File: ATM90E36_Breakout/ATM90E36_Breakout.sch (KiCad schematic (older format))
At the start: 70 parts, among them IC1 ATM90E36, Q1 FA-128

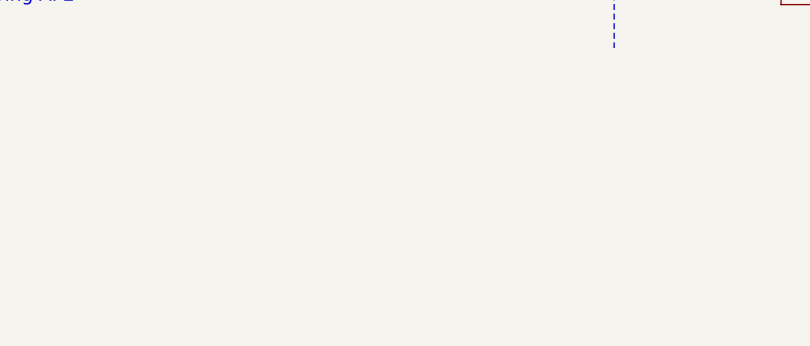
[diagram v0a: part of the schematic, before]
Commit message: Fix up silk screens
Signed-off-by: Tisham Dhar <whatnickd@gmail.com>
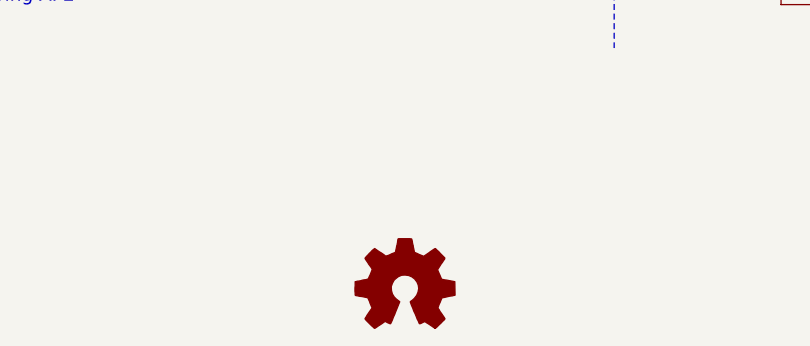
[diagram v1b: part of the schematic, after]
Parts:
- added LOGO1: Logo_Open_Hardware_Small, ATM90E36_Breakout:OSHW-LOGO-M, symbol Graphic:Logo_Open_Hardware_Small
- IC1: manf# (none) -> ATM90E36A-AU-R
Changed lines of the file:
@@
 F 2 "ATM90E36_Breakout:TQFP48" H 7200 3800 50  0001 C CNN
 F 3 "" H 7200 3800 50  0001 C CNN
+F 4 "	ATM90E36A-AU-R" H 7200 3800 50  0001 C CNN "manf#"
 	1    7200 3800
 	1    0    0    -1
@@
 Wire Notes Line
 	9420 750  9420 6990
+$Comp
+L Graphic:Logo_Open_Hardware_Small LOGO1
+U 1 1 5E08577C
+P 8505 8045
+F 0 "LOGO1" H 8505 8320 50  0001 C CNN
+F 1 "Logo_Open_Hardware_Small" H 8505 7820 50  0001 C CNN
+F 2 "ATM90E36_Breakout:OSHW-LOGO-M" H 8505 8045 50  0001 C CNN
+F 3 "~" H 8505 8045 50  0001 C CNN
+	1    8505 8045
+	1    0    0    -1
+$EndComp
 $EndSCHEMATC

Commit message: Add full BOM and Gerbers
Signed-off-by: Tisham Dhar <whatnickd@gmail.com>
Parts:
- added Hole0, Hole1, Hole2, Hole3: MountingHole, MountingHole:MountingHole_2.2mm_M2, symbol Mechanical:MountingHole
- C1, C10, C11, C14, C16, C2, C20, C3, C4, C5, C6, C7, C8, C9: manf# (none) -> C0603C183K5RACTU
- C12, C19: manf# (none) -> GRM21BR61E106MA73L
- C13, C15, C17, C18, C21: manf# (none) -> C0603C104K5RAC3190
- CTA1, CTB1, CTC1, CTN1: manf# (none) -> ST-PJ-312
- DMA1, JP1, JP2, JP3, LOGO1, PM0, PM1: DNP (none) -> (none)
- LED1: manf# (none) -> LTST-C193KRKT-5A
- LED2: value GRN -> RED; manf# (none) -> LTST-C193KRKT-5A
- LED3: value BLU -> RED; manf# (none) -> LTST-C193KRKT-5A
- LED4: value YEL -> RED; manf# (none) -> LTST-C193KRKT-5A
- Q1: manf# (none) -> FA-128 16.00M-A0NNNNHB0REB
- R1, R15, R16, R17, R18, R2, R3, R4: manf# (none) -> CRL0603-FW-2R40ELF
- R10, R12, R14: manf# (none) -> RC0603FR-07100KL
- R11, R13, R19, R20, R21, R22, R23, R24, R25, R5, R6, R7, R8, R9: manf# (none) -> RT0603FRE071KL
- R26: manf# (none) -> SR0603KR-7W10KL
- R27: manf# (none) -> YC164-JR-071KL
- R36: manf# (none) -> YC164-JR-0710KL
- UAUB1, UCUN1: manf# (none) -> 20020327-C021B01LF
- ZX0, ZX2: value ZX0 -> ZX; DNP (none) -> (none)
- ZX1: value ZX1 -> ZX; DNP (none) -> (none)

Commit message: Update parts for availability
Signed-off-by: Tisham Dhar <whatnickd@gmail.com>
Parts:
- CTA1, CTB1, CTC1, CTN1: manf# ST-PJ-312 -> ST-PJ-342
- Q1: manf# FA-128 16.00M-A0NNNNHB0REB -> ECS-160-10-36-CKM-TR
- R26: manf# SR0603KR-7W10KL -> RC0201JR-0710KL
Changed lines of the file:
@@
 F 2 "ATM90E36_Breakout:R0603" H 7390 1100 50  0001 C CNN
 F 3 "" H 7390 1100 50  0001 C CNN
-F 4 "SR0603KR-7W10KL" H 7390 1100 50  0001 C CNN "manf#"
+F 4 "RC0201JR-0710KL" H 7390 1100 50  0001 C CNN "manf#"
 	1    7390 1100
 	-1   0    0    1
@@
 F 2 "ATM90E36_Breakout:FA-128" H 7460 5890 50  0001 C CNN
 F 3 "" H 7460 5890 50  0001 C CNN
-F 4 "FA-128 16.00M-A0NNNNHB0REB" H 7460 5890 50  0001 C CNN "manf#"
+F 4 "ECS-160-10-36-CKM-TR" H 7460 5890 50  0001 C CNN "manf#"
 	1    7460 5890
 	1    0    0    -1
@@
 F 2 "ATM90E36_Breakout:AUDIO6P-SMD-3.5-14.0X6.4X5.0MM" H 10060 1500 50  0001 C CNN
 F 3 "" H 10060 1500 50  0001 C CNN
-F 4 "ST-PJ-312" H 10060 1500 50  0001 C CNN "manf#"
+F 4 "ST-PJ-342" H 10060 1500 50  0001 C CNN "manf#"
 	1    10060 1500
 	0    -1   -1   0
@@
 F 2 "ATM90E36_Breakout:AUDIO6P-SMD-3.5-14.0X6.4X5.0MM" H 11100 1500 50  0001 C CNN
 F 3 "" H 11100 1500 50  0001 C CNN
-F 4 "ST-PJ-312" H 11100 1500 50  0001 C CNN "manf#"
+F 4 "ST-PJ-342" H 11100 1500 50  0001 C CNN "manf#"
 	1    11100 1500
 	0    -1   -1   0
@@
 F 2 "ATM90E36_Breakout:AUDIO6P-SMD-3.5-14.0X6.4X5.0MM" H 10000 3120 50  0001 C CNN
 F 3 "" H 10000 3120 50  0001 C CNN
-F 4 "ST-PJ-312" H 10000 3120 50  0001 C CNN "manf#"
+F 4 "ST-PJ-342" H 10000 3120 50  0001 C CNN "manf#"
 	1    10000 3120
 	0    -1   -1   0
@@
 F 2 "ATM90E36_Breakout:AUDIO6P-SMD-3.5-14.0X6.4X5.0MM" H 11040 3110 50  0001 C CNN
 F 3 "" H 11040 3110 50  0001 C CNN
-F 4 "ST-PJ-312" H 11040 3110 50  0001 C CNN "manf#"
+F 4 "ST-PJ-342" H 11040 3110 50  0001 C CNN "manf#"
 	1    11040 3110
 	0    -1   -1   0

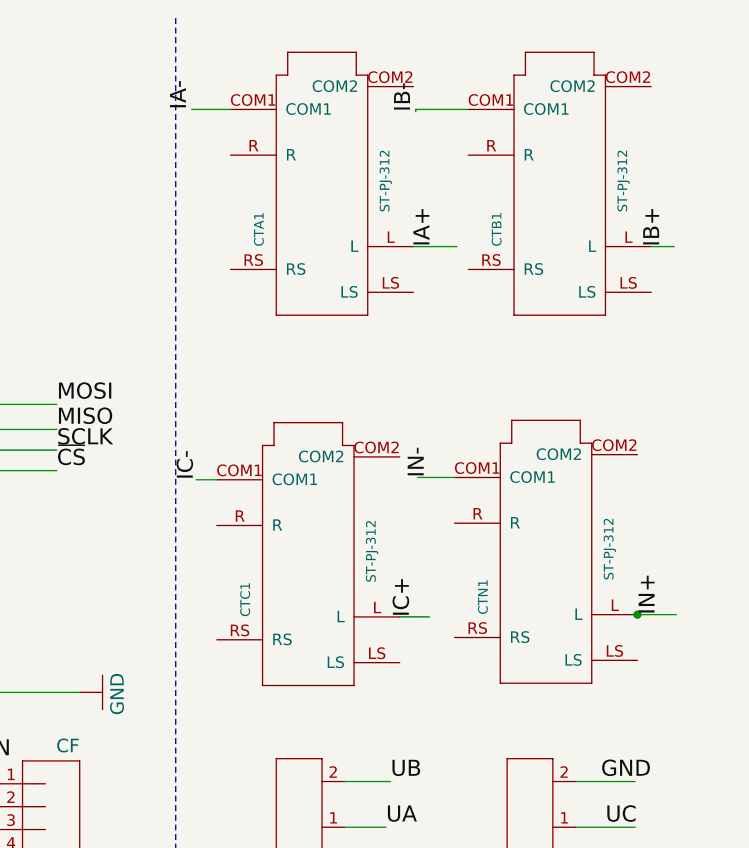
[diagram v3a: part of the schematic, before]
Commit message: Updated Stereojacks to mainstream ones
Signed-off-by: Tisham Dhar <whatnickd@gmail.com>
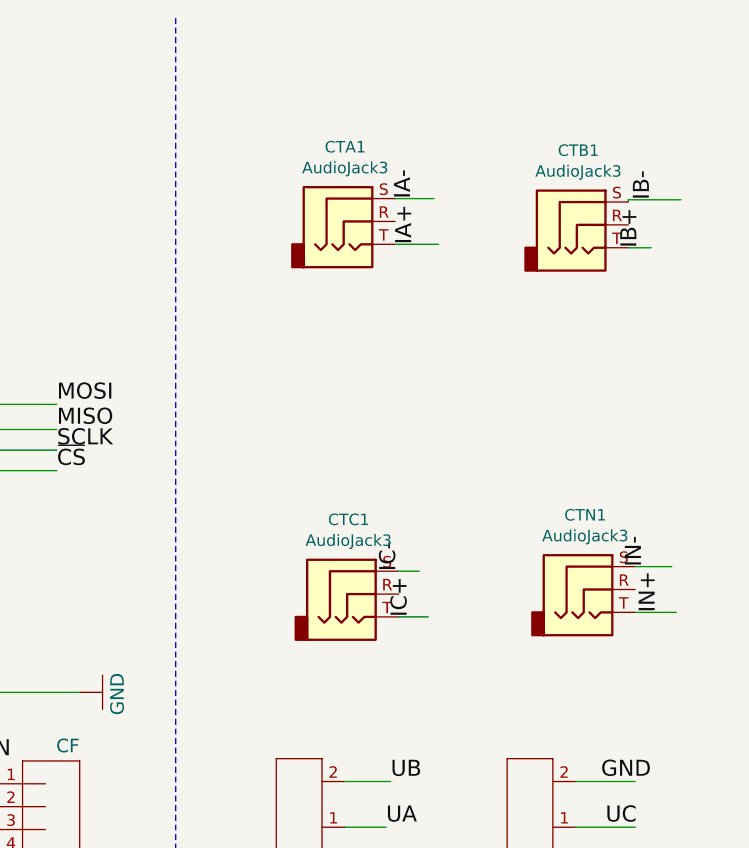
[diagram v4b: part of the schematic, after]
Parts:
- removed CTA1, CTB1, CTC1, CTN1: ST-PJ-312, ATM90E36_Breakout:AUDIO6P-SMD-3.5-14.0X6.4X5.0MM, symbol ATM90E36_Breakout-eagle-import:AUDIO-JACK-6P-SMD(ST-PJ-312)
- added CTA1, CTB1, CTC1, CTN1: AudioJack3, Connector_Audio:Jack_3.5mm_CUI_SJ-3523-SMT_Horizontal, symbol Connector:AudioJack3
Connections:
- wire segments 282 -> 281
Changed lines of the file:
@@
 IB-
 Wire Wire Line
-	10700 1150 10470 1150
-Wire Wire Line
-	10470 1150 10470 1160
-Text Label 10470 1160 1    70   ~ 0
+	11630 1545 11400 1545
+Wire Wire Line
+	11400 1545 11400 1555
+Text Label 11515 1545 1    70   ~ 0
 IB-
 Wire Wire Line
@@
 IA+
 Wire Wire Line
-	10460 1750 10650 1750
-Text Label 10555 1750 1    70   ~ 0
+	10380 1740 10570 1740
+Text Label 10475 1740 1    70   ~ 0
 IA+
 Wire Wire Line
@@
 IB+
 Wire Wire Line
-	11500 1750 11600 1750
-Text Label 11560 1750 1    70   ~ 0
+	11400 1755 11500 1755
+Text Label 11460 1755 1    70   ~ 0
 IB+
 Wire Wire Line
@@
 IC+
 Wire Wire Line
-	10400 3370 10530 3370
-Text Label 10465 3370 1    70   ~ 0
-IC+
+	10395 3370 10525 3370
 Wire Wire Line
 	3600 4300 3700 4300
@@
 Connection ~ 3200 5600
 Text Label 2900 5600 2    70   ~ 0
-IC-
-Wire Wire Line
-	9600 2770 9510 2770
-Text Label 9520 2770 1    70   ~ 0
 IC-
 Wire Wire Line
@@
 Text Label 3000 6000 2    70   ~ 0
 IN+
-Wire Wire Line
-	11430 3360 11440 3360
-Wire Wire Line
-	11440 3360 11610 3360
-Text Label 11540 3360 1    70   ~ 0
+Text Label 11540 3350 1    70   ~ 0
 IN+
-Connection ~ 11440 3360
 Wire Wire Line
 	3200 7300 3200 7200
@@
 IN-
 Wire Wire Line
-	10640 2760 10480 2760
-Text Label 10530 2760 1    70   ~ 0
+	11590 3150 11430 3150
+Text Label 11480 3150 1    70   ~ 0
 IN-
 Wire Wire Line
@@
 Connection ~ 1600 5600
 Text Label 1300 5600 2    70   ~ 0
-IA-
-Wire Wire Line
-	9660 1150 9490 1150
-Text Label 9490 1150 1    70   ~ 0
 IA-
 Wire Wire Line
@@
 	1    10970 4190
 	-1   0    0    1
-$EndComp
-$Comp
-L ATM90E36_Breakout-eagle-import:AUDIO-JACK-6P-SMD(ST-PJ-312) CTA1
-U 1 1 5E8BFF6F
-P 10060 1500
-F 0 "CTA1" H 9810 1750 42  0000 L BNN
-F 1 "ST-PJ-312" H 9960 1200 42  0000 L BNN
-F 2 "ATM90E36_Breakout:AUDIO6P-SMD-3.5-14.0X6.4X5.0MM" H 10060 1500 50  0001 C CNN
-F 3 "" H 10060 1500 50  0001 C CNN
-F 4 "ST-PJ-342" H 10060 1500 50  0001 C CNN "manf#"
-	1    10060 1500
-	0    -1   -1   0
-$EndComp
-$Comp
-L ATM90E36_Breakout-eagle-import:AUDIO-JACK-6P-SMD(ST-PJ-312) CTB1
-U 1 1 61C5C6F3
-P 11100 1500
-F 0 "CTB1" H 10850 1750 42  0000 L BNN
-F 1 "ST-PJ-312" H 11000 1200 42  0000 L BNN
-F 2 "ATM90E36_Breakout:AUDIO6P-SMD-3.5-14.0X6.4X5.0MM" H 11100 1500 50  0001 C CNN
-F 3 "" H 11100 1500 50  0001 C CNN
-F 4 "ST-PJ-342" H 11100 1500 50  0001 C CNN "manf#"
-	1    11100 1500
-	0    -1   -1   0
-$EndComp
-$Comp
-L ATM90E36_Breakout-eagle-import:AUDIO-JACK-6P-SMD(ST-PJ-312) CTC1
-U 1 1 53035BF0
-P 10000 3120
-F 0 "CTC1" H 9750 3370 42  0000 L BNN
-F 1 "ST-PJ-312" H 9900 2820 42  0000 L BNN
-F 2 "ATM90E36_Breakout:AUDIO6P-SMD-3.5-14.0X6.4X5.0MM" H 10000 3120 50  0001 C CNN
-F 3 "" H 10000 3120 50  0001 C CNN
-F 4 "ST-PJ-342" H 10000 3120 50  0001 C CNN "manf#"
-	1    10000 3120
-	0    -1   -1   0
-$EndComp
-$Comp
-L ATM90E36_Breakout-eagle-import:AUDIO-JACK-6P-SMD(ST-PJ-312) CTN1
-U 1 1 80D53B8A
-P 11040 3110
-F 0 "CTN1" H 10790 3360 42  0000 L BNN
-F 1 "ST-PJ-312" H 10940 2810 42  0000 L BNN
-F 2 "ATM90E36_Breakout:AUDIO6P-SMD-3.5-14.0X6.4X5.0MM" H 11040 3110 50  0001 C CNN
-F 3 "" H 11040 3110 50  0001 C CNN
-F 4 "ST-PJ-342" H 11040 3110 50  0001 C CNN "manf#"
-	1    11040 3110
-	0    -1   -1   0
 $EndComp
 $Comp
@@
 	1    0    0    -1
 $EndComp
+$Comp
+L Connector:AudioJack3 CTB1
+U 1 1 5E171051
+P 11200 1655
+F 0 "CTB1" H 11182 1980 50  0000 C CNN
+F 1 "AudioJack3" H 11182 1889 50  0000 C CNN
+F 2 "Connector_Audio:Jack_3.5mm_CUI_SJ-3523-SMT_Horizontal" H 11200 1655 50  0001 C CNN
+F 3 "~" H 11200 1655 50  0001 C CNN
+F 4 "SJ-3523-SMT-TR" H 11200 1655 50  0001 C CNN "manf#"
+	1    11200 1655
+	1    0    0    -1
+$EndComp
+$Comp
+L Connector:AudioJack3 CTC1
+U 1 1 5E171794
+P 10195 3270
+F 0 "CTC1" H 10177 3595 50  0000 C CNN
+F 1 "AudioJack3" H 10177 3504 50  0000 C CNN
+F 2 "Connector_Audio:Jack_3.5mm_CUI_SJ-3523-SMT_Horizontal" H 10195 3270 50  0001 C CNN
+F 3 "~" H 10195 3270 50  0001 C CNN
+F 4 "SJ-3523-SMT-TR" H 10195 3270 50  0001 C CNN "manf#"
+	1    10195 3270
+	1    0    0    -1
+$EndComp
+$Comp
+L Connector:AudioJack3 CTN1
+U 1 1 5E1722BE
+P 11230 3250
+F 0 "CTN1" H 11212 3575 50  0000 C CNN
+F 1 "AudioJack3" H 11212 3484 50  0000 C CNN
+F 2 "Connector_Audio:Jack_3.5mm_CUI_SJ-3523-SMT_Horizontal" H 11230 3250 50  0001 C CNN
+F 3 "~" H 11230 3250 50  0001 C CNN
+F 4 "SJ-3523-SMT-TR" H 11230 3250 50  0001 C CNN "manf#"
+	1    11230 3250
+	1    0    0    -1
+$EndComp
+Wire Wire Line
+	11430 3350 11610 3350
+Text Label 10455 3370 1    70   ~ 0
+IC+
+Wire Wire Line
+	10485 3170 10395 3170
+Text Label 10405 3170 1    70   ~ 0
+IC-
+$Comp
+L Connector:AudioJack3 CTA1
+U 1 1 5E1708FD
+P 10180 1640
+F 0 "CTA1" H 10162 1965 50  0000 C CNN
+F 1 "AudioJack3" H 10162 1874 50  0000 C CNN
+F 2 "Connector_Audio:Jack_3.5mm_CUI_SJ-3523-SMT_Horizontal" H 10180 1640 50  0001 C CNN
+F 3 "~" H 10180 1640 50  0001 C CNN
+F 4 "SJ-3523-SMT-TR" H 10180 1640 50  0001 C CNN "manf#"
+	1    10180 1640
+	1    0    0    -1
+$EndComp
+Text Label 10470 1540 1    70   ~ 0
+IA-
+Wire Wire Line
+	10550 1540 10380 1540
 $EndSCHEMATC

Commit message: Fix BOM part
Signed-off-by: Tisham Dhar <whatnickd@gmail.com>
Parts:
- R26: manf# RC0201JR-0710KL -> RC0603JR-0710KL
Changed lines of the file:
@@
 F 2 "ATM90E36_Breakout:R0603" H 7390 1100 50  0001 C CNN
 F 3 "" H 7390 1100 50  0001 C CNN
-F 4 "RC0201JR-0710KL" H 7390 1100 50  0001 C CNN "manf#"
+F 4 "RC0603JR-0710KL" H 7390 1100 50  0001 C CNN "manf#"
 	1    7390 1100
 	-1   0    0    1
